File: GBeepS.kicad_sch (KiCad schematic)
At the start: 35 parts, among them J1 Ant, U1 NCP160xMX, U2 MMC3416xPJ, U3 ZOE-M8Q

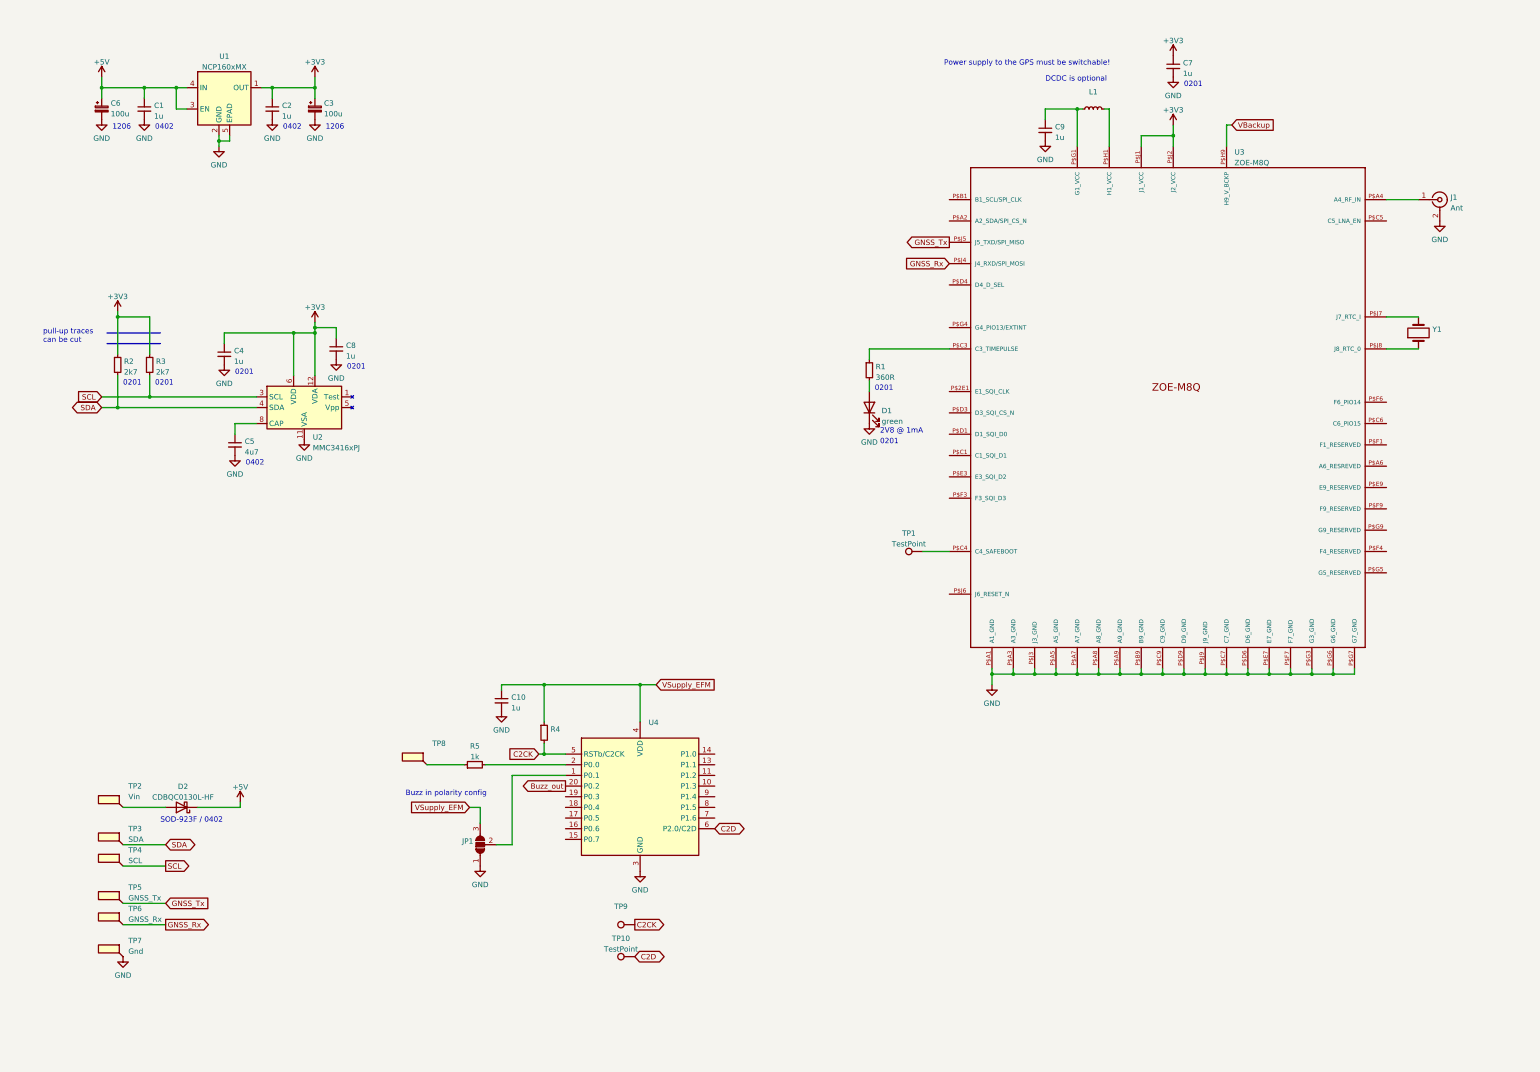
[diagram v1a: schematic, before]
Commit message: added battery stuff
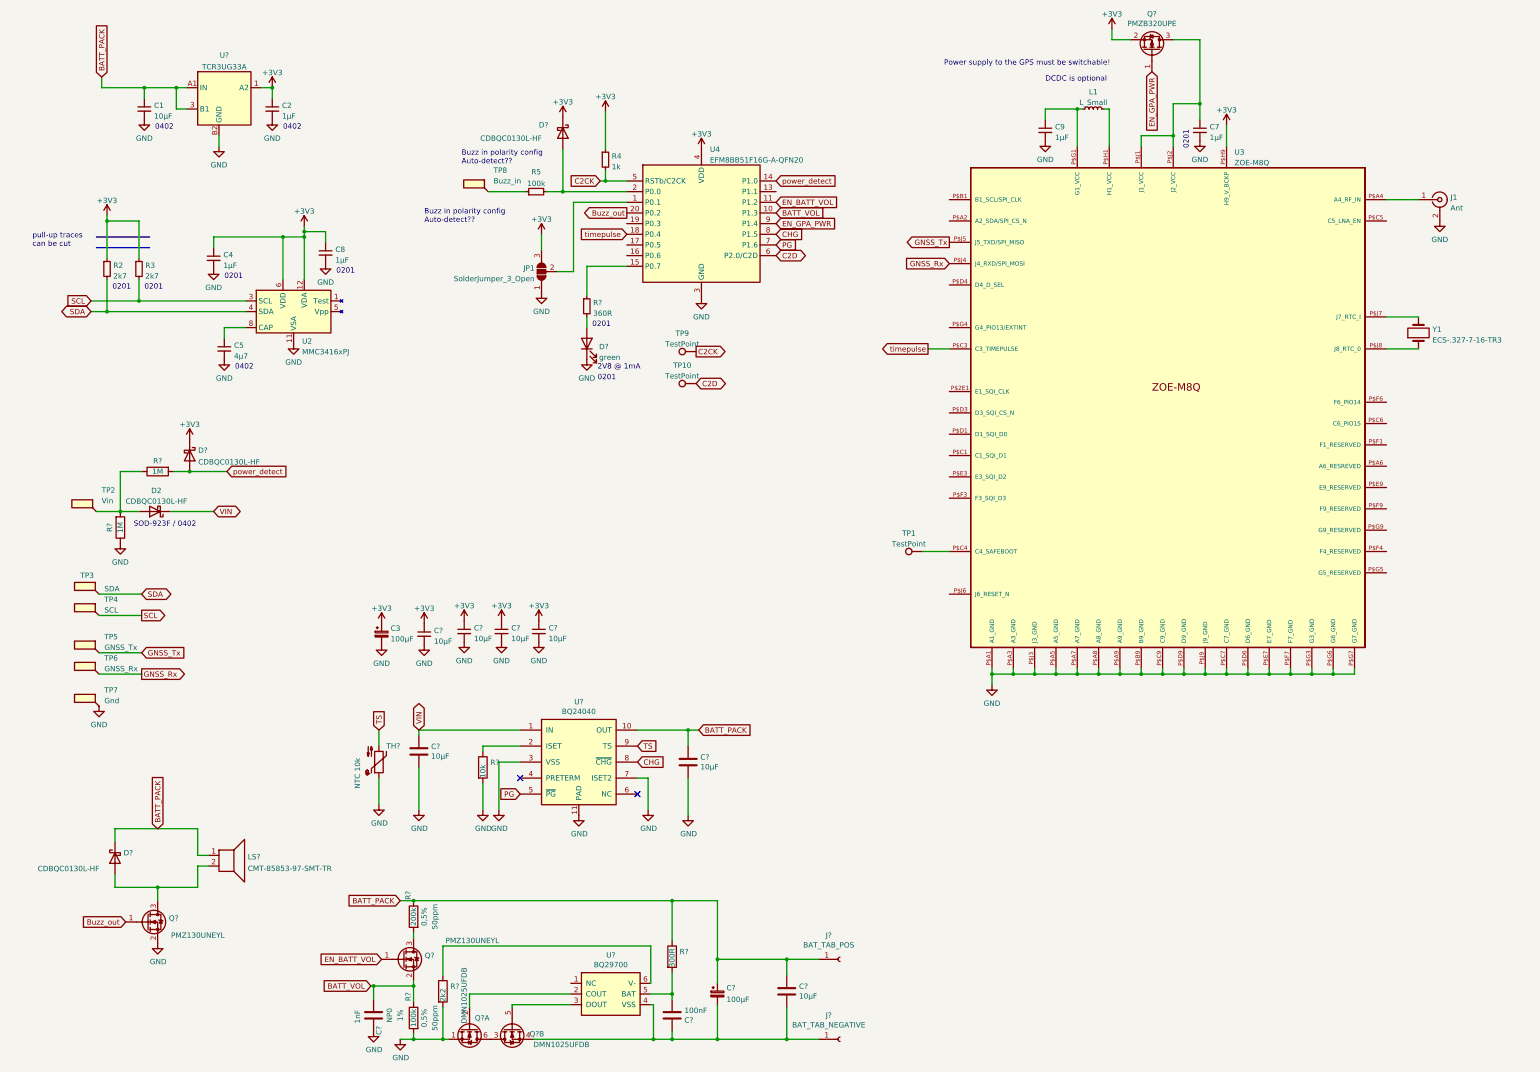
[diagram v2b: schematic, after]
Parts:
- removed C10: 1u, Yolo-GPS:C_0201_0603Metric_mod, symbol Device:C_Small
- removed C6: 100u, Capacitor_Tantalum_SMD:CP_EIA-3216-18_Kemet-A, symbol Device:C_Polarized_Small
- removed D1: green, LED_SMD:LED_0201_0603Metric, symbol Device:LED
- removed R1: 360R, Yolo-GPS:R_0201_0603Metric_mod, symbol Device:R_Small
- removed U1: NCP160xMX, Yolo-GPS:OnSemi-XDFN-4-1EP_1x1mm_P0.65mm_EP0.52x0.52mm, symbol HypaLoc:NCP160xMX
- added C? (x4): 10µF, Capacitor_SMD:C_0402_1005Metric, symbol Device:C_Small
- added C?: 100µF, Capacitor_Tantalum_SMD:CP_EIA-3216-18_Kemet-A, symbol Device:C_Polarized_Small
- added C?: 1nF, Yolo-GPS:C_0201_0603Metric_mod, symbol Device:C
- added C?: 100nF, Yolo-GPS:C_0201_0603Metric_mod, symbol Device:C
- added C? (x3): 10µF, Capacitor_SMD:C_0402_1005Metric, symbol Device:C
- added D? (x3): CDBQC0130L-HF, Yolo-GPS:D_SOD-932F_0402_1005Metric, symbol Device:D_Schottky
- added D?: green, LED_SMD:LED_0201_0603Metric, symbol Device:LED
- added J?: BAT_TAB_POS, symbol Connector:Conn_01x01_Female
- added J?: BAT_TAB_NEGATIVE, symbol Connector:Conn_01x01_Female
- added LS?: CMT-85853-97-SMT-TR, Buzzer_Beeper:MagneticBuzzer_CUI_CMT-8504-100-SMT, symbol Device:Speaker
- added Q? (x2): PMZ130UNEYL, Package_DFN_QFN:Diodes_DFN1006-3, symbol Device:Q_NMOS_GSD
- added Q? (x2): DMN1025UFDB, Yolo-GPS:U-DFN2020-6-2EP, symbol Device:Q_DUAL_NMOS_S1G1D2S2G2D1
- added Q?: PMZB320UPE, Package_DFN_QFN:Diodes_DFN1006-3, symbol Device:Q_PMOS_GSD
- added R? (x2): 1M, Yolo-GPS:R_0201_0603Metric_mod, symbol Device:R
- added R?: 300R, Yolo-GPS:R_0201_0603Metric_mod, symbol Device:R
- added R?: 100k, Yolo-GPS:R_0201_0603Metric_mod, symbol Device:R
- added R?: 10k, Yolo-GPS:R_0201_0603Metric_mod, symbol Device:R
- added R?: 2k2, Yolo-GPS:R_0201_0603Metric_mod, symbol Device:R
- added R?: 200k, Yolo-GPS:R_0201_0603Metric_mod, symbol Device:R
- added R?: 360R, Yolo-GPS:R_0201_0603Metric_mod, symbol Device:R_Small
- added TH?: NTC 10k, Resistor_SMD:R_0402_1005Metric, symbol Device:Thermistor_NTC
- added U?: TCR3UG33A, Package_BGA:WLP-4_0.73x0.73mm_Layout2x2_P0.35mm_Ball0.22mm_Pad0.2mm_NSMD, symbol HypaLoc:TCR3UG33A
- added U?: BQ24040, Yolo-GPS:WSON_10_P0.4_2x2, symbol HypaLoc:BQ24040
- added U?: BQ29700, Package_SON:WSON-6_1.5x1.5mm_P0.5mm, symbol HypaLoc:BQ29700
- C1: value 1u -> 10µF
- C2: value 1u -> 1µF; footprint Capacitor_SMD:C_0402_1005Metric -> Yolo-GPS:C_0201_0603Metric_mod
- C3: value 100u -> 100µF
- C4, C7, C8, C9: value 1u -> 1µF
- C5: value 4u7 -> 4µ7
- JP1: value (none) -> SolderJumper_3_Open; footprint (none) -> Jumper:SolderJumper-3_P1.3mm_Open_RoundedPad1.0x1.5mm
- L1: value (none) -> L_Small; footprint (none) -> Inductor_SMD:L_1008_2520Metric
- R4: value (none) -> 1k; footprint (none) -> Yolo-GPS:R_0201_0603Metric_mod
- R5: value 1k -> 100k
- TP8: value (none) -> Buzz_in; footprint (none) -> Yolo-GPS:pad_1x1.5
- TP9: value (none) -> TestPoint; footprint (none) -> TestPoint:TestPoint_Pad_D1.0mm
- U3: footprint Yolo-GPS:ZOE-M8 -> ZOE-M8
- U4: value (none) -> EFM8BB51F16G-A-QFN20; footprint (none) -> Package_DFN_QFN:SiliconLabs_QFN-20-1EP_3x3mm_P0.5mm_EP1.8x1.8mm
- Y1: value (none) -> ECS-.327-7-16-TR3; footprint (none) -> Crystal:Crystal_SMD_MicroCrystal_CM9V-T1A-2Pin_1.6x1.0mm
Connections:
- net VBackup is gone; now on net +3V3: U3.P$H9 (H9_V_BCKP)
- net VSupply_EFM is gone; now on net +3V3: JP1.3 (B), R4.1, U4.4 (VDD)
- net +3V3: now also C?.1, C?.1, C?.1, C?.1, D?.1 (K), D?.1 (K), Q?.2 (S), U?.1 (A2); no longer C7.1, U3.P$J1 (J1_VCC), U3.P$J2 (J2_VCC)
- net Buzz_out: now also Q?.1 (G)
- net GND: now also C?.2, C?.2, C?.2, C?.2, C?.2, C?.2, C?.2, D?.1 (K), Q?.1 (S), Q?.2 (S), R?.1, R?.2, R?.2, R?.2, TH?.1, U?.11 (PAD), U?.3 (VSS), U?.7 (ISET2), U?.B2 (GND)
- net BATT_VOL: now reaches U4.10 (P1.3)
- net BATT_VOL: now also C?.1, Q?.2 (S), R?.1
- net EN_BATT_VOL: now reaches U4.11 (P1.2)
- net EN_BATT_VOL: now also Q?.1 (G)
- net power_detect: now reaches U4.14 (P1.0)
- net power_detect: now also D?.2 (A), R?.2
- net at U4.15 (P0.7): now also R?.1
- net timepulse: now reaches U4.18 (P0.4)
- net timepulse: now also U3.P$C3 (C3_TIMEPULSE)
- net at R5.2, U4.2 (P0.0): now also D?.2 (A)
- net PG: now reaches U4.7 (P1.6)
- net PG: now also U?.5 (~{PG})
- net CHG: now reaches U4.8 (P1.5)
- net CHG: now also U?.8 (~{CHG})
- net EN_GPA_PWR: now reaches U4.9 (P1.4)
- net EN_GPA_PWR: now also Q?.1 (G)
- net at D2.2 (A), TP2.1: now also R?.1, R?.2
- net +5V renamed BATT_PACK
- net BATT_PACK: now also C?.1, C?.1, C?.1, D?.1 (K), J?.1 (Pin_1), LS?.1, R?.1, R?.1, U?.10 (OUT), U?.3 (B1), U?.A1 (IN); no longer D2.1 (K)
- new net: D?.2 (A), LS?.2, Q?.3 (D)
- new net: C?.1, C?.2, C?.2, J?.1 (Pin_1), Q?.4 (S), U?.4 (VSS)
- new net: D?.2 (A), R?.2
- new net: C7.1, Q?.3 (D), U3.P$J1 (J1_VCC), U3.P$J2 (J2_VCC)
- new net: C?.2, R?.2, U?.5 (BAT)
- new net: Q?.3 (D), R?.2
- new net: R?.1, U?.2 (ISET)
- new net: Q?.2 (G), U?.2 (COUT)
- new net: Q?.3 (D), Q?.6 (D)
- new net: Q?.5 (G), U?.3 (DOUT)
- new net: R?.1, U?.6 (V-)
- new net TS: TH?.2, U?.9 (TS)
- new net VIN: C?.1, D2.1 (K), U?.1 (IN)
- no-connect marks 0 -> 2
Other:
- note added: "Buzz in polarity config Auto-detect??"
- note removed: "1206"
- note removed: "Buzz in polarity config"
- moved on the sheet: C3, C4, C5, C7, C8, D2, JP1, R2, R3, R4, R5, TP10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

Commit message: rudimentary layout and 3D models
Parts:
- added H1, H2, H3, H4: MountingHole, MountingHole:MountingHole_2.2mm_M2_DIN965_Pad, symbol Mechanical:MountingHole
- J2, J3: renamed from J?; footprint (none) -> MountingHole:MountingHole_2.2mm_M2_DIN965_Pad
- gave numbers to parts that had none: 31
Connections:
- net +3V3: now also U1.A2 (OUT); no longer U1.1 (A2)
- net BATT_PACK: now also U1.B1 (EN); no longer U1.3 (B1)

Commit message: update layout
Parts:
- U1: value TCR3UG33A -> (none); footprint Package_BGA:WLP-4_0.73x0.73mm_Layout2x2_P0.35mm_Ball0.22mm_Pad0.2mm_NSMD -> (none)
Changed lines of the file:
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@@
     (in_bom yes) (on_board yes) (fields_autoplaced)
     (property "Reference" "U1" (id 0) (at 62.23 27.8343 0))
-    (property "Value" "TCR3UG33A" (id 1) (at 62.23 30.6094 0))
-    (property "Footprint" "Package_BGA:WLP-4_0.73x0.73mm_Layout2x2_P0.35mm_Ball0.22mm_Pad0.2mm_NSMD" (id 2) (at 62.23 38.1 0)
+    (property "Value" "" (id 1) (at 62.23 30.6094 0))
+    (property "Footprint" "" (id 2) (at 62.23 38.1 0)
       (effects (font (size 1.27 1.27)) hide)
     )
@@
     (pin "2")
     (pin "6")
+    (pin "3")
+    (pin "4")
+    (pin "5")
   )
   (symbol (lib_id "HypaLoc:BQ29700") (at 154.94 251.46 0) (unit 1)
@@
       (effects (font (size 1.27 1.27)) hide)
     )
+    (pin "1")
+    (pin "2")
+    (pin "6")
     (pin "3")
     (pin "4")
@@
     )
     (path "/456045c7-119b-443f-9d83-8a11e699febc"
-      (reference "U1") (unit 1) (value "TCR3UG33A") (footprint "Package_BGA:WLP-4_0.73x0.73mm_Layout2x2_P0.35mm_Ball0.22mm_Pad0.2mm_NSMD")
+      (reference "U1") (unit 1) (value "TCR3UG33A") (footprint "Yolo-GPS:WLP-4_0.73x0.73mm_Layout2x2_P0.35mm_Ball0.22mm_Pad0.2mm_NSMD_mod")
     )
     (path "/e51acd71-fc05-40a6-92da-13a5f86fa2a6"

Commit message: started routing
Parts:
- removed JP1: SolderJumper_3_Open, Jumper:SolderJumper-3_P1.3mm_Open_RoundedPad1.0x1.5mm, symbol Jumper:SolderJumper_3_Open
- C7, C9: value 1µF -> 10µF; footprint Yolo-GPS:C_0201_0603Metric_mod -> Capacitor_SMD:C_0402_1005Metric
- L1: value L_Small -> MCHK1608T1R5MKN; footprint Inductor_SMD:L_1008_2520Metric -> Inductor_SMD:L_0603_1608Metric
- U1: value (none) -> TCR3UG33A; footprint (none) -> Yolo-GPS:WLP-4_0.73x0.73mm_Layout2x2_P0.35mm_Ball0.22mm_Pad0.2mm_NSMD_mod
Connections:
- net Buzz_out: now also U4.19 (P0.3); no longer U4.20 (P0.2)
- net SCL: now also U4.1 (P0.1)
- net SDA: now also U4.20 (P0.2)
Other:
- note added: "dismount resistors for pullup deactivation"
- note removed: "pull-up traces can be cut"

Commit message: saved schematic
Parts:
- removed C8: 1µF, Yolo-GPS:C_0201_0603Metric_mod, symbol Device:C_Small
- removed H2, H3: MountingHole, MountingHole:MountingHole_2.2mm_M2_DIN965_Pad, symbol Mechanical:MountingHole
- added Q5: PMZB320UPE, Package_DFN_QFN:Diodes_DFN1006-3, symbol Device:Q_PMOS_GSD
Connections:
- net +3V3: now also Q5.2 (S); no longer C4.1, U2.12 (VDA), U2.6 (VDD)
- net CHG: now also U4.14 (P1.0); no longer U4.8 (P1.5)
- net GND: now also LS1.3 (2), LS1.4 (2)
- net PG: now also U4.13 (P1.1); no longer U4.7 (P1.6)
- net SCL: now also U4.17 (P0.5); no longer U4.1 (P0.1)
- net power_detect: now also U4.8 (P1.5); no longer U4.14 (P1.0)
- net timepulse: now also U4.7 (P1.6); no longer U4.18 (P0.4)
- new net: C4.1, Q5.3 (D), U2.12 (VDA), U2.6 (VDD)
- new net EN_PWR_MAG: Q5.1 (G), U4.18 (P0.4)
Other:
- note added: "Buzz in polarity config Auto-detect or I2C config!"
- note removed: "Buzz in polarity config Auto-detect??"
